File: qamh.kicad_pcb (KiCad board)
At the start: 2 copper layers, 32.7 x 128.5 mm, 19 parts, among them J1 Eurorack_Power_16pin_Shrouded, J2 OUTPUT, J3 INPUT 1, J4 INPUT 2, J5 INPUT 3, J6 Conn_01x02_Pin

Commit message: routing
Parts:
- added R2: 10k, Resistor_THT:R_Axial_DIN0204_L3.6mm_D1.6mm_P7.62mm_Horizontal, F.Cu at (228.6, 94.0)
- added SW1: SW_Push, Button_Switch_THT:SW_PUSH_6mm_H5mm, F.Cu at (222.1, 83.1)
- moved R1 51.9 mm to (203.2, 128.3)
- moved C1 44.6 mm to (208.4, 88.9), turned to 0 degrees
- moved J6 18.8 mm to (204.5, 90.2)
- moved D6 8.89 mm to (228.6, 105.4)
- moved D2 5.08 mm to (228.6, 116.8)
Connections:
- A2 pad D2: unconnected-(A2-D2_INT0-PadD2) -> Net-(A2-D2_INT0)
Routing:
- net Net-(J2-PadT): track 12.9 -> 61.5 mm
- net Net-(A2-D2_INT0): track 0.00 -> 32.6 mm
- net +5V: track 128.9 -> 150.0 mm
- net Net-(A2-D11_MOSI): track 63.1 -> 50.1 mm
- net GND: track 232.7 -> 224.6 mm
- net Net-(J6-Pin_2): track 14.5 -> 22.3 mm
- net Net-(D1-A): track 134.1 -> 131.8 mm
- net Net-(A2-PadA0): track 35.6 -> 36.9 mm
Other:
- board text added: "QAMH, v0.2-pm"
- board text removed: "QAMH, v0.1-pm"

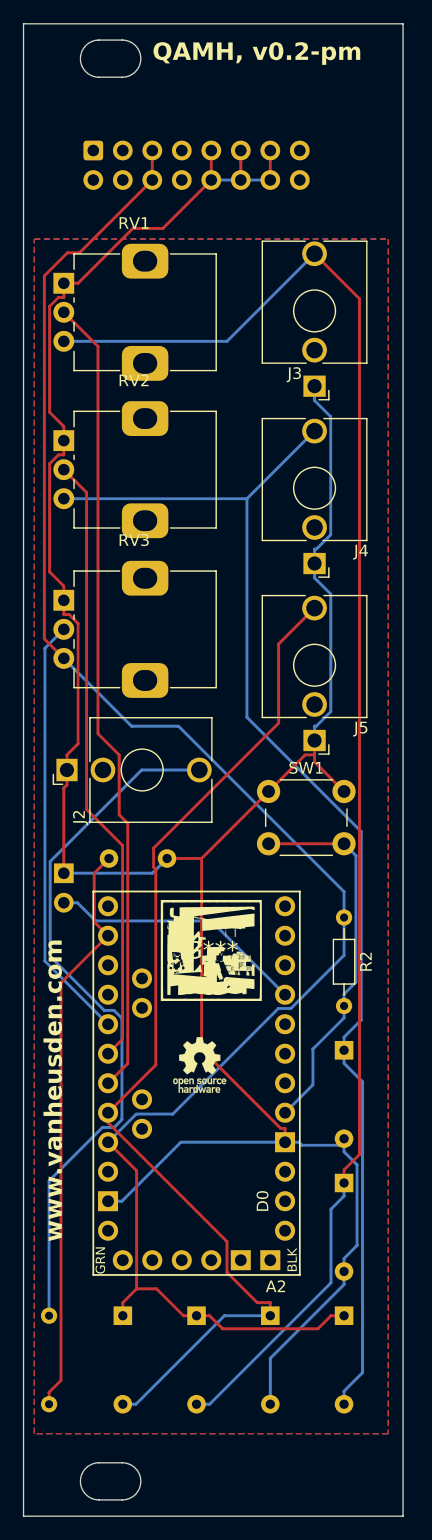
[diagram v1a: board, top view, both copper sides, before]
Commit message: header for plug/unplug 5V
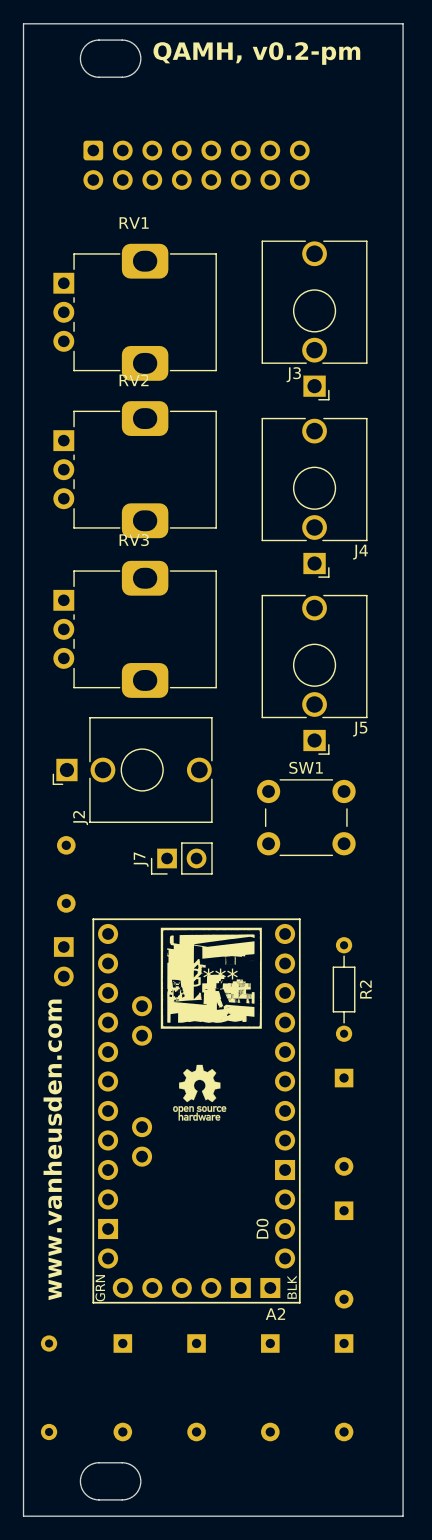
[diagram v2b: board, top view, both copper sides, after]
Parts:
- added J7: Conn_01x02_Pin, Connector_PinHeader_2.54mm:PinHeader_1x02_P2.54mm_Vertical, F.Cu at (213.4, 88.9)
- moved J6 6.35 mm to (204.5, 96.5)
- moved C1 5.34 mm to (204.7, 92.8), turned to 90 degrees
- moved G*** 2.39 mm to (217.2, 99.2)
- moved A2 2.39 mm to (215.9, 110.6)
- moved D1 2.39 mm to (215.9, 130.7)
- moved D2 2.39 mm to (228.6, 119.2)
- moved D3 2.39 mm to (209.6, 130.7)
- moved D4 2.39 mm to (222.2, 130.7)
- moved D5 2.39 mm to (228.6, 130.7)
- moved D6 2.39 mm to (228.6, 107.8)
- moved R1 2.39 mm to (203.2, 130.7)
- moved R2 2.39 mm to (228.6, 96.4)
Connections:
- A2 pad Vcc1: +5V -> Net-(J7-Pin_1)
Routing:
- net GND: track 224.6 -> 0.00 mm
- net +5V: track 150.0 -> 0.00 mm
- net Net-(D1-A): track 131.8 -> 0.00 mm
- net Net-(D5-A): track 108.0 -> 0.00 mm
- net Net-(D3-A): track 90.8 -> 0.00 mm
- net Net-(A2-PadA2): track 69.4 -> 0.00 mm
- net Net-(J2-PadT): track 61.5 -> 0.00 mm
- net Net-(A2-PadA1): track 52.9 -> 0.00 mm
- net Net-(A2-D11_MOSI): track 50.1 -> 0.00 mm
- net Net-(A2-PadA0): track 36.9 -> 0.00 mm
- net Net-(A2-D2_INT0): track 32.6 -> 0.00 mm
- net Net-(J6-Pin_2): track 22.3 -> 0.00 mm
- removed copper zone on B.Cu, net GND
- removed copper zone on F.Cu, net GND
